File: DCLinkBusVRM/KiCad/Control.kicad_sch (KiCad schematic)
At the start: 50 parts, among them IC1 UCC28220D, IC2 LM358DR, IC3 UCC27424QDRQ1, Q3 SIHFR120-GE3

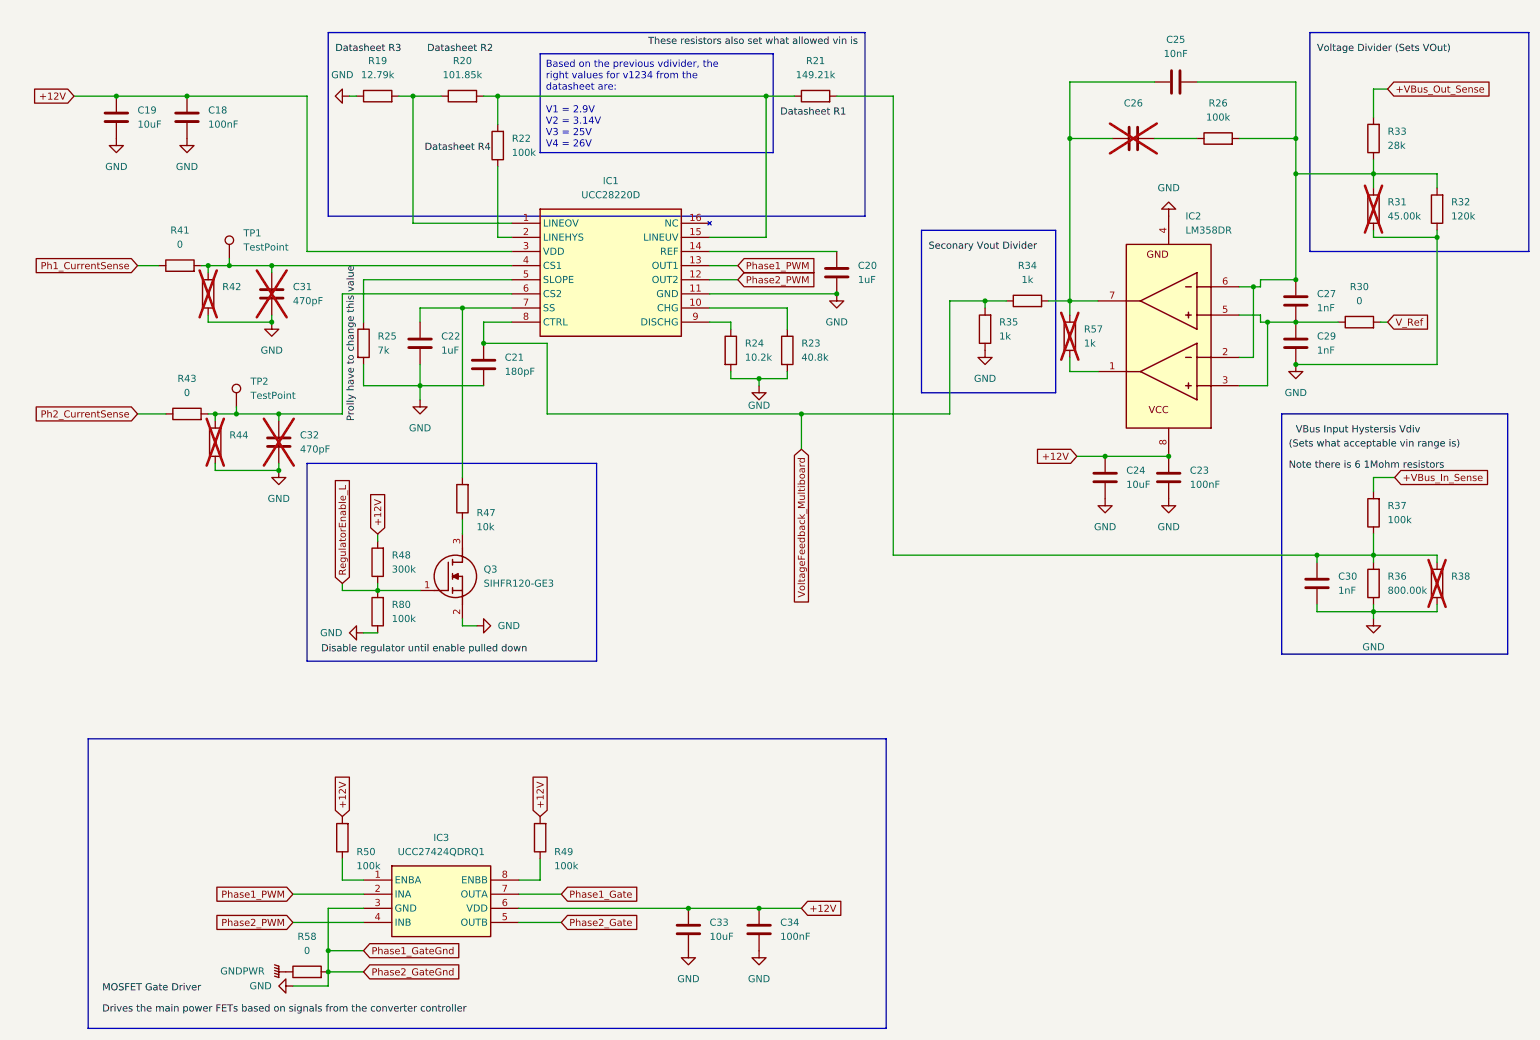
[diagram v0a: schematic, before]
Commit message: Update boost converter, add dynamic brake grid, etc
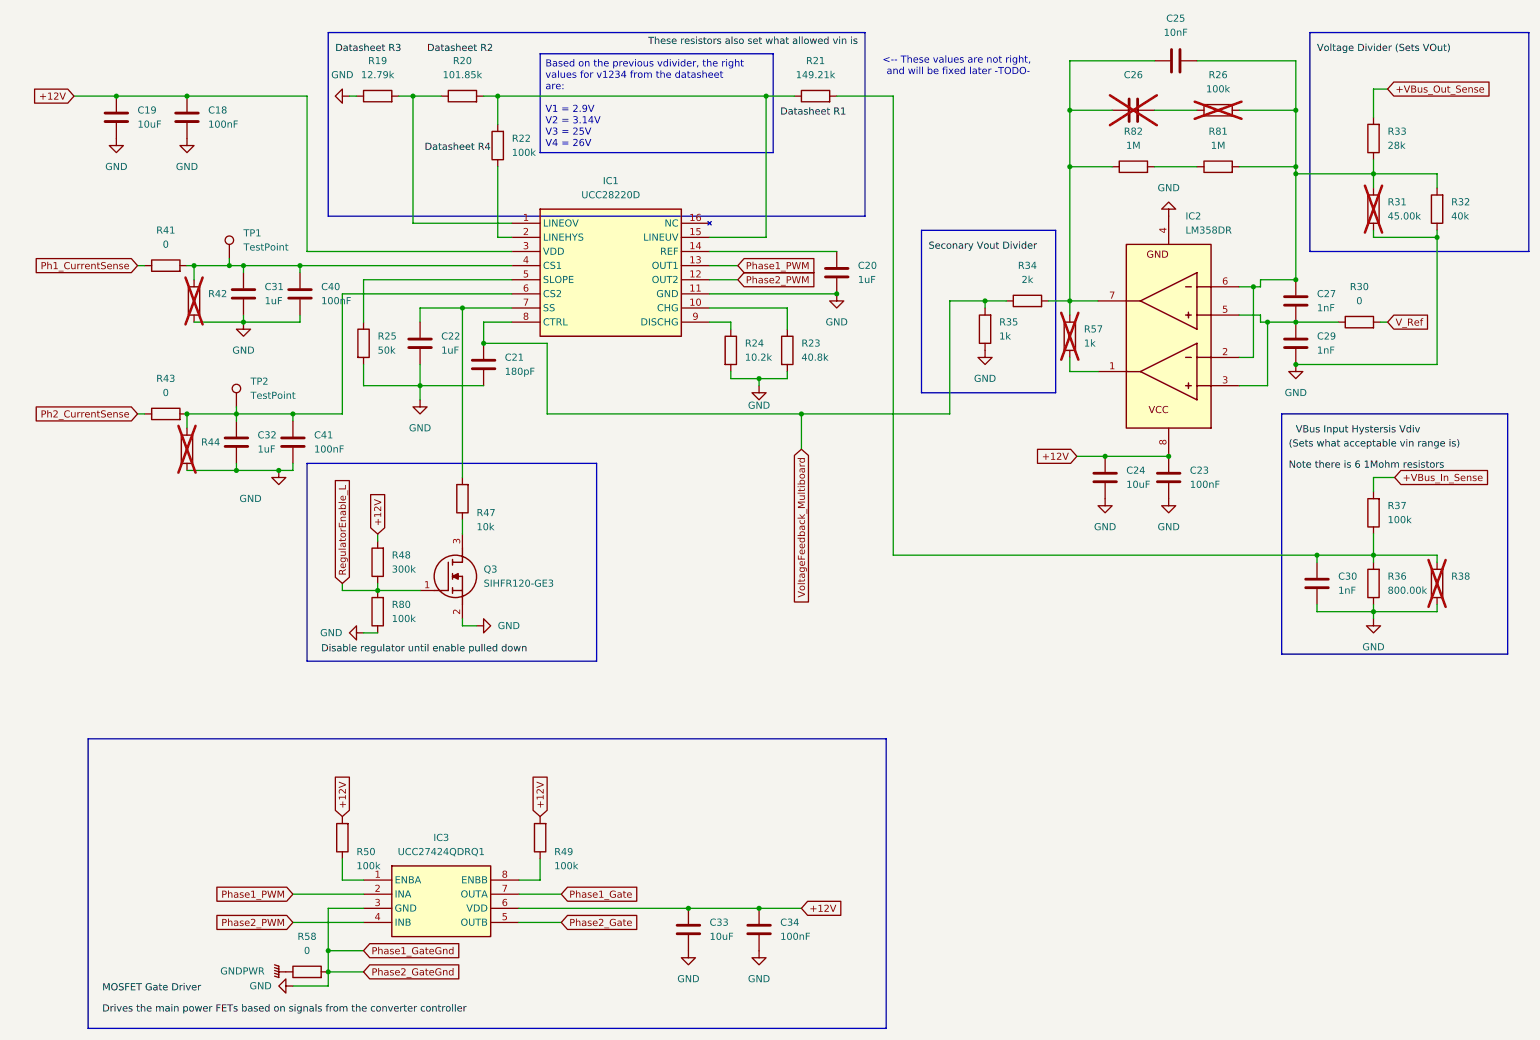
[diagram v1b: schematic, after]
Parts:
- added C40, C41: 100nF, Capacitor_SMD:C_1210_3225Metric_Pad1.33x2.70mm_HandSolder, symbol Device:C
- added R81, R82: 1M, Resistor_SMD:R_1210_3225Metric_Pad1.30x2.65mm_HandSolder, symbol Device:R
- C31, C32: value 470pF -> 1uF; now fitted
- R25: value 7k -> 50k
- R26: now not fitted
- R32: value 120k -> 40k
- R34: value 1k -> 2k
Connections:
- net GND: now also C40.2, C41.2
- net at C25.1, C26.1, IC2.7 (OUT2)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: now also R82.1
- net at C25.2, C27.2, IC2.2 (IN1-)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: now also R81.2
- net at C31.1, IC1.4 (CS1), R41.2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: now also C40.1
- net at C32.1, IC1.6 (CS2), R43.2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: now also C41.1
- new net: R81.1, R82.2
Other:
- note added: "<-- These values are not right, and will be fixed later -TODO-"
- moved on the sheet: C25, C26, R41, R42, R43, R44

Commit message: Update Canbus protocol for vrm
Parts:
- removed C30: 1nF, Capacitor_SMD:C_1210_3225Metric_Pad1.33x2.70mm_HandSolder, symbol Device:C
- removed R20: 101.85k, Resistor_SMD:R_1210_3225Metric_Pad1.30x2.65mm_HandSolder, symbol Device:R
- removed R21: 149.21k, Resistor_SMD:R_1210_3225Metric_Pad1.30x2.65mm_HandSolder, symbol Device:R
- removed R22, R37: 100k, Resistor_SMD:R_1210_3225Metric_Pad1.30x2.65mm_HandSolder, symbol Device:R
- removed R36: 800.00k, Resistor_SMD:R_1210_3225Metric_Pad1.30x2.65mm_HandSolder, symbol Device:R
- removed R38: ~, Resistor_SMD:R_1210_3225Metric_Pad1.30x2.65mm_HandSolder, symbol Device:R
- added R84, R87: 2k, Resistor_SMD:R_1210_3225Metric_Pad1.30x2.65mm_HandSolder, symbol Device:R
- added R86: 1k, Resistor_SMD:R_1210_3225Metric_Pad1.30x2.65mm_HandSolder, symbol Device:R
- added R88: ~, Resistor_SMD:R_1210_3225Metric_Pad1.30x2.65mm_HandSolder, symbol Device:R
- R19: value 12.79k -> 4.7k
- R23: value 40.8k -> 43k
- R24: value 10.2k -> 10k
- R32: value 40k -> 43k
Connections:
- net GND: now also R86.1
- net at IC1.1 (LINEOV), R19.2: now also R88.2
- net at IC1.15 (LINEUV): now also R84.1, R86.2, R87.2, R88.1
- net at IC1.2 (LINEHYS): now also R87.1
- new net +5V: R84.2
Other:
- note added: "We disable the chips vin sense we do that with the mcu instead"
- note removed: "<-- These values are not right, and will be fixed later -TODO-"
- moved on the sheet: R33
